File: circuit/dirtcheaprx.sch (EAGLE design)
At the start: 20 parts, among them IC1 MCP1700

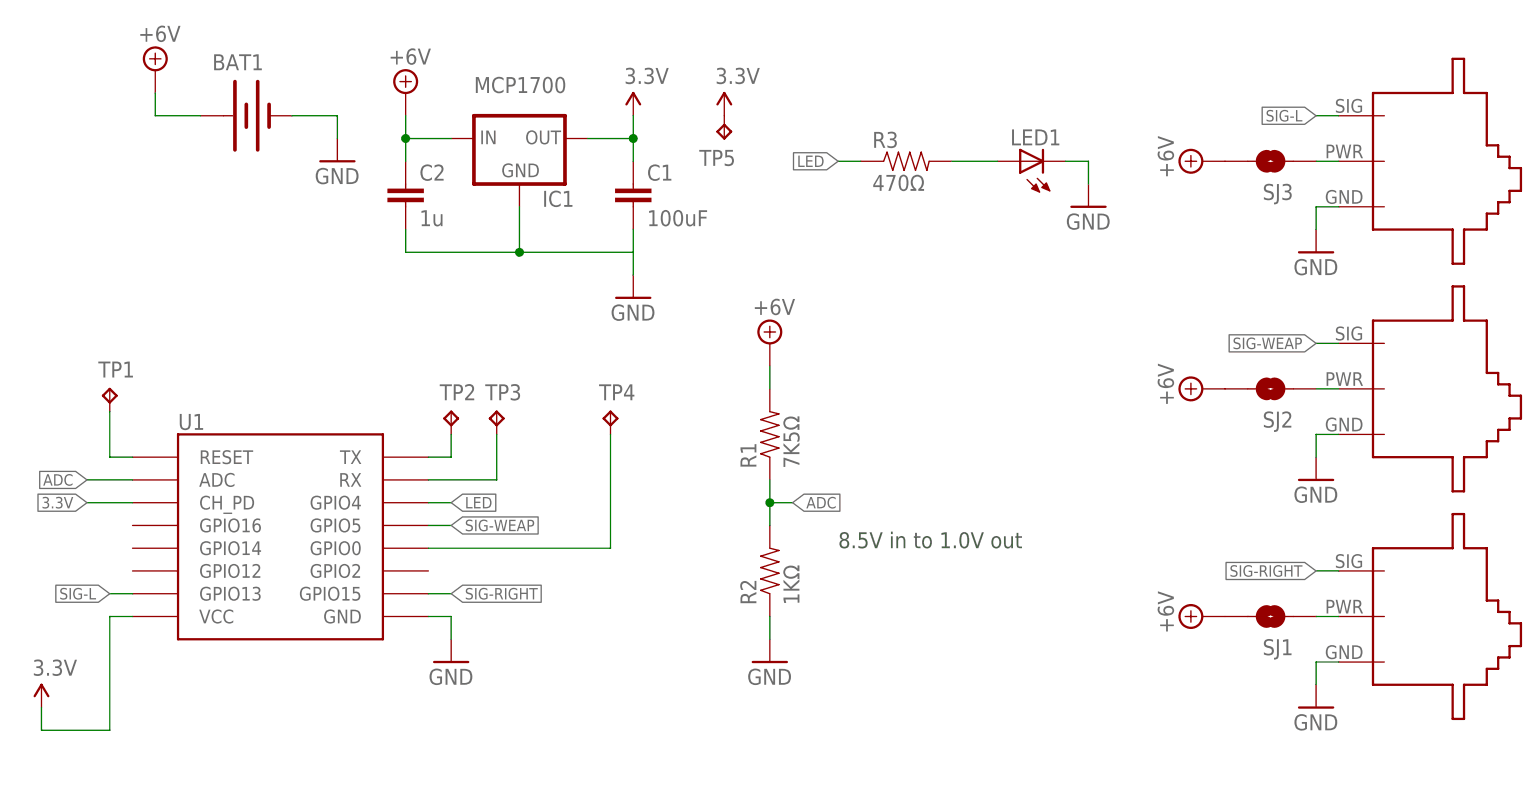
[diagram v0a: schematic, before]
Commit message: GPIO15 needs to be pulled down, I missed the memo...
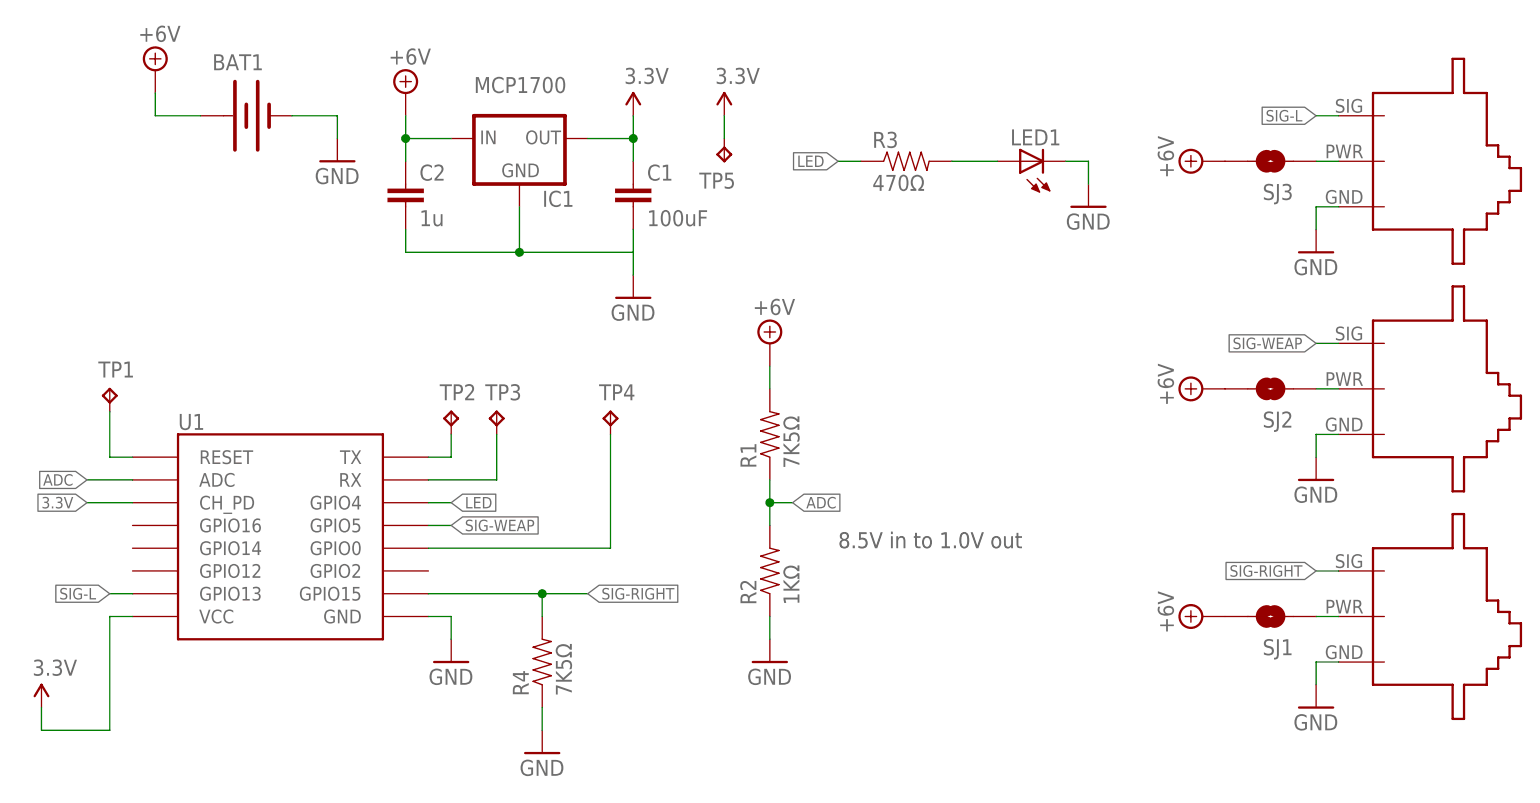
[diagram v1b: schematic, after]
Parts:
- added R4: 7K5Ω, dirtcheaprx:RESISTOR0603-RES
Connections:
- net GND: now also R4.1
- net SIG-RIGHT: now also R4.2
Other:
- moved on the sheet: TP5
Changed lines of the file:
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@@
 <part name="SUPPLY5" library="dirtcheaprx" deviceset="+6V" device=""/>
 <part name="SUPPLY6" library="dirtcheaprx" deviceset="+6V" device=""/>
+<part name="R4" library="dirtcheaprx" deviceset="RESISTOR" device="0603-RES" value="7K5Ω"/>
+<part name="GND9" library="dirtcheaprx" deviceset="GND" device=""/>
 </parts>
 <sheets>
@@
 <instance part="TP4" gate="G$1" x="40.64" y="2.54"/>
 <instance part="GND8" gate="1" x="93.98" y="25.4"/>
-<instance part="TP5" gate="G$1" x="53.34" y="33.02" rot="R180"/>
+<instance part="TP5" gate="G$1" x="53.34" y="30.48" rot="R180"/>
 <instance part="P+3" gate="G$1" x="53.34" y="35.56"/>
 <instance part="SUPPLY4" gate="G$1" x="106.68" y="-20.32" rot="R90"/>
 <instance part="SUPPLY5" gate="G$1" x="106.68" y="5.08" rot="R90"/>
 <instance part="SUPPLY6" gate="G$1" x="106.68" y="30.48" rot="R90"/>
+<instance part="R4" gate="G$1" x="33.02" y="-25.4" rot="R90"/>
+<instance part="GND9" gate="1" x="33.02" y="-35.56"/>
 </instances>
 <busses>
@@
 <pinref part="TP5" gate="G$1" pin="TP"/>
 <pinref part="P+3" gate="G$1" pin="3.3V"/>
+<wire x1="53.34" y1="33.02" x2="53.34" y2="35.56" width="0.1524" layer="91"/>
 </segment>
 </net>
@@
 <wire x1="93.98" y1="30.48" x2="93.98" y2="27.94" width="0.1524" layer="91"/>
 </segment>
+<segment>
+<pinref part="GND9" gate="1" pin="GND"/>
+<pinref part="R4" gate="G$1" pin="1"/>
+<wire x1="33.02" y1="-33.02" x2="33.02" y2="-30.48" width="0.1524" layer="91"/>
+</segment>
 </net>
 <net name="ADC" class="0">
@@
 <segment>
 <pinref part="U1" gate="G$1" pin="GPIO15"/>
-<wire x1="20.32" y1="-17.78" x2="22.86" y2="-17.78" width="0.1524" layer="91"/>
-<label x="22.86" y="-17.78" size="1.27" layer="95" xref="yes"/>
-</segment>
-</net>
+<wire x1="20.32" y1="-17.78" x2="33.02" y2="-17.78" width="0.1524" layer="91"/>
+<label x="38.1" y="-17.78" size="1.27" layer="95" xref="yes"/>
+<pinref part="R4" gate="G$1" pin="2"/>
+<wire x1="33.02" y1="-17.78" x2="38.1" y2="-17.78" width="0.1524" layer="91"/>
+<wire x1="33.02" y1="-20.32" x2="33.02" y2="-17.78" width="0.1524" layer="91"/>
+<junction x="33.02" y="-17.78"/>
+</segment>
+</net>

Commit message: corrected GPIO4 and GPIO5 mixup in PCBs
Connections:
- net LED: now also U1.GPIO5; no longer U1.GPIO4
- net SIG-WEAP: now also U1.GPIO4; no longer U1.GPIO5
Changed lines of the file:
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@@
 <net name="LED" class="0">
 <segment>
-<pinref part="U1" gate="G$1" pin="GPIO4"/>
+<pinref part="U1" gate="G$1" pin="GPIO5"/>
 <wire x1="20.32" y1="-7.62" x2="22.86" y2="-7.62" width="0.1524" layer="91"/>
 <label x="22.86" y="-7.62" size="1.27" layer="95" xref="yes"/>
@@
 </segment>
 <segment>
-<pinref part="U1" gate="G$1" pin="GPIO5"/>
+<pinref part="U1" gate="G$1" pin="GPIO4"/>
 <wire x1="20.32" y1="-10.16" x2="22.86" y2="-10.16" width="0.1524" layer="91"/>
 <label x="22.86" y="-10.16" size="1.27" layer="95" xref="yes"/>
